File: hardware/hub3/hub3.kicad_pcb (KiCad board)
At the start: 2 copper layers, 42 x 42 mm, 11 parts, among them J1 LCD0, J2 LCD1, J3 LCD2, U1 74HC138, U2 XIAO ESP32S3

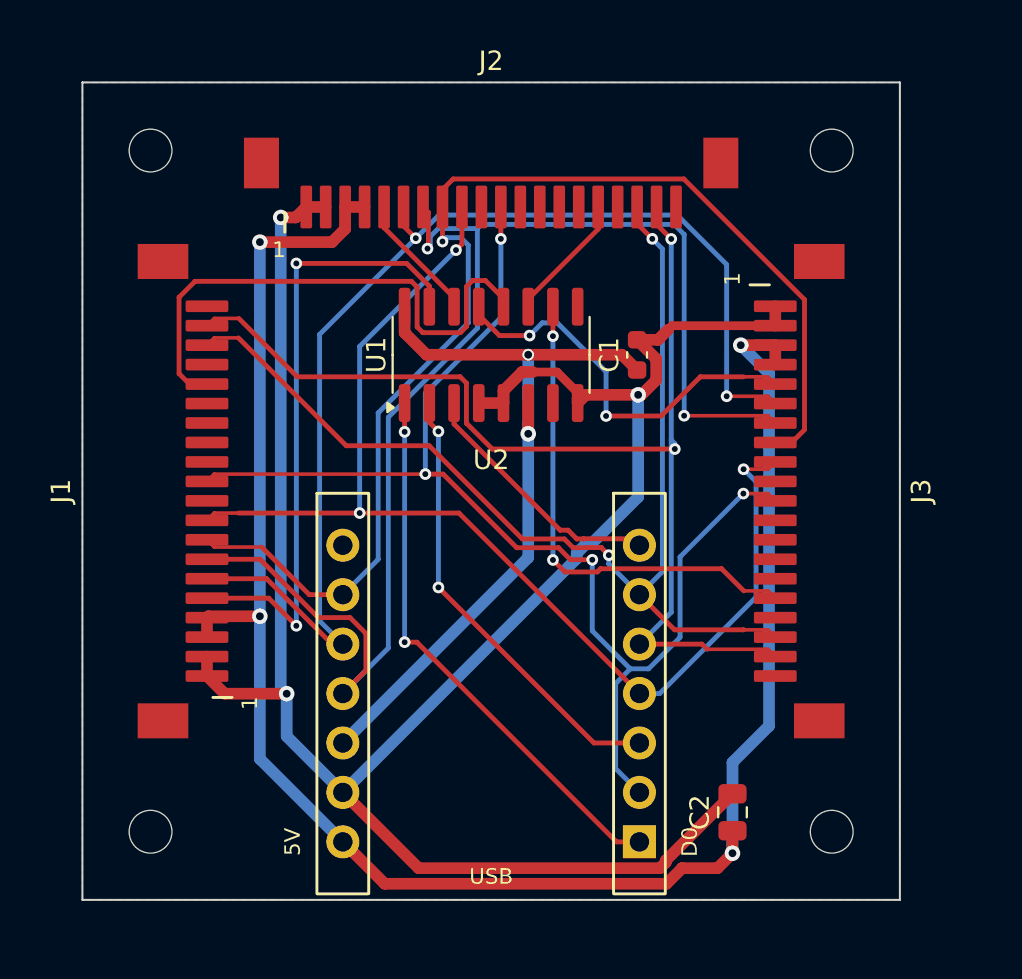
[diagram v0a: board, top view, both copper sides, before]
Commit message: hub3: route until clean, and write the JLCPCB files
Freerouting gives a different routing each run and now and then leaves
an island, a gap or a long neck on a power track, so route.py routes
again in a fresh process until KiCad's DRC is clean and the +5V and
+3V3 necks add up to 5 mm or less. GND pads join the pours directly.
fab.py writes the Gerbers, drill files, BOM and placement from the
board's lower left corner. Record why the FFC pin order is 1 to 1.

Claude-Session: https://claude.ai/code/session_01QQqL2MiTqB6ZDq8JiNUdWg
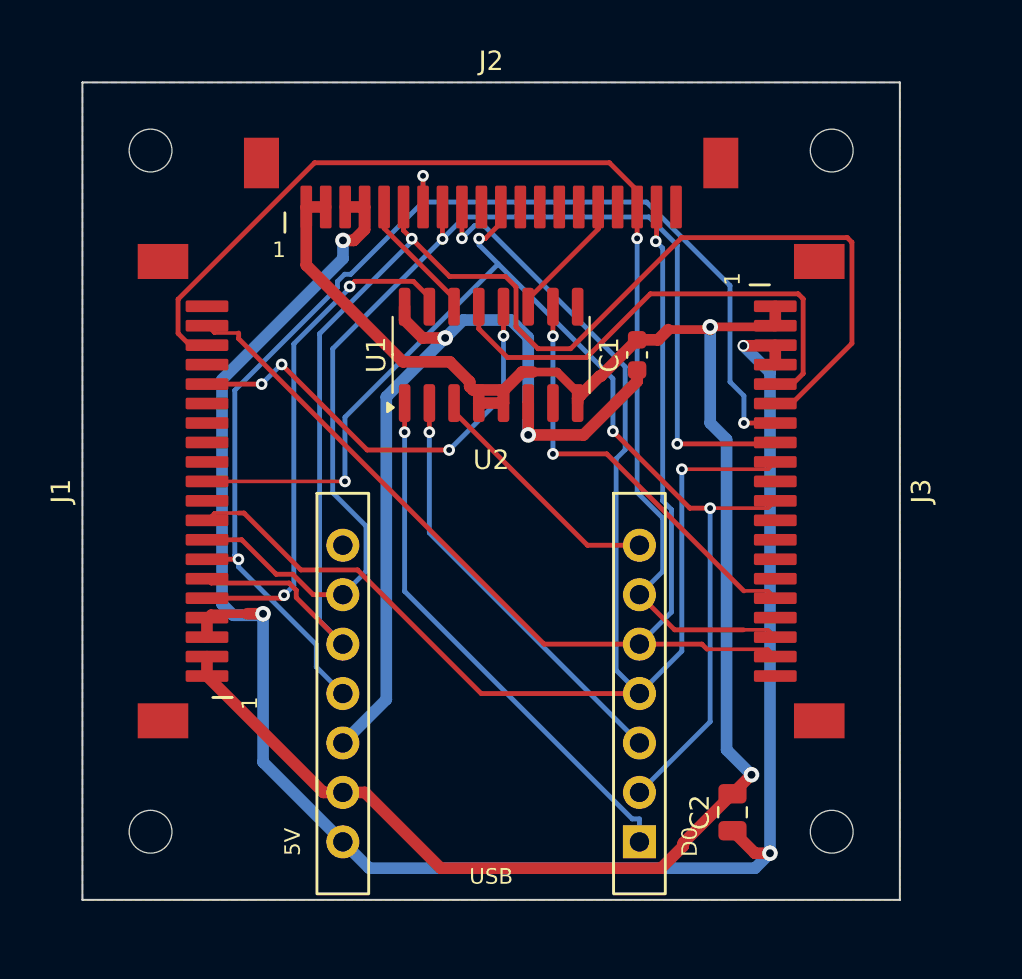
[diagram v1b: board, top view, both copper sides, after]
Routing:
- net GND: track 111.6 -> 95.8 mm, vias 3 -> 2
- net BL_CTRL: track 60.8 -> 74.3 mm, vias 3 -> 2
- net LCM_SDO: track 60.6 -> 72.7 mm, vias 2 -> 1
- net LCM_SDI: track 70.7 -> 62.8 mm, vias 2 -> 3
- net LCM_SCS0: track 32.2 -> 26.3 mm
- net +3V3: track 39.6 -> 45.1 mm
- net LCD_CS0: track 28.0 -> 23.2 mm, vias 0 -> 4
- net LCM_SCS2: track 20.7 -> 25.4 mm, vias 2 -> 0
- net LCD_CS2: track 25.4 -> 22.1 mm
- net LCD_DIN: track 56.9 -> 60.3 mm, vias 2 -> 1
- net +5V: track 96.1 -> 99.0 mm
- net LCM_SCLK: track 62.9 -> 60.0 mm, vias 1 -> 2
- net LCM_RESET: track 64.4 -> 62.8 mm
- net SEL_B: track 23.3 -> 21.9 mm, vias 2 -> 1
- net SEL_A: track 28.6 -> 27.8 mm, vias 2 -> 1
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
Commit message: hub3: use the Ckmtw C132515 FFC connector, 44 mm board
C132515 has JLCPCB's own EasyEDA footprint, so the pads come from it
rather than from pixels of a drawing. Its body is 2.5 mm longer, so the
board grows to 44 mm to keep the corners clear. Move the 10 uF next to
the XIAO 5V pin.

route.py now starts each attempt from an unrouted copy that make.py
leaves in build/ with the project beside it (without it pcbnew used the
default net classes and saved them over the project), and when an
attempt is not clean it makes the board again: Freerouting routes the
same DSN the same way whatever its options, but each make.py run gives
a different DSN. Allow 7.5 mm of necked power track, about 2.5 mm per
connector.

Claude-Session: https://claude.ai/code/session_01QQqL2MiTqB6ZDq8JiNUdWg
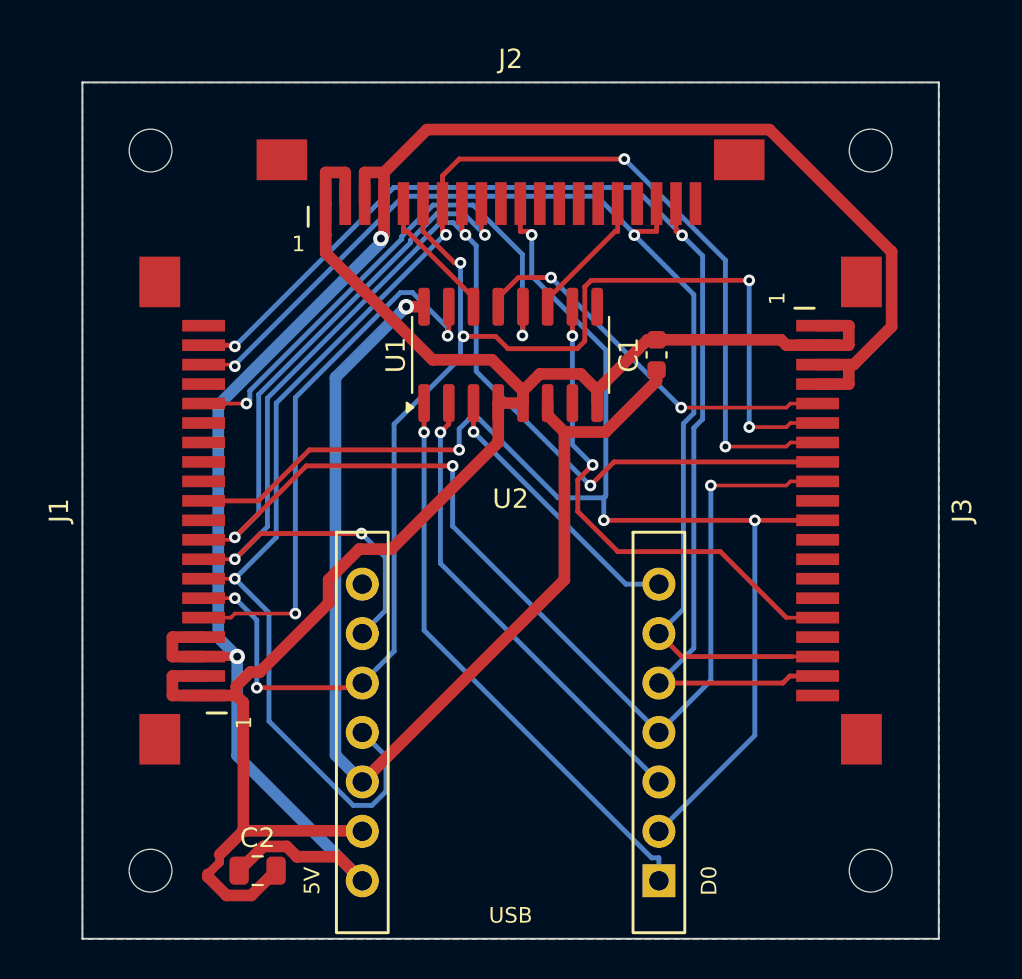
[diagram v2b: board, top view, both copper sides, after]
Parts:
- J1, J2, J3: footprint cubic-earth:FFC_1.0mm_20P_Bottom_C2998680 -> cubic-earth:FFC_1.0mm_20P_Bottom_C132515
- moved C2 24.6 mm to (109.0, 140.5), turned to 0 degrees
- moved H4 2.83 mm to (140.5, 140.5)
- moved J3 2.33 mm to (138.6, 122.0)
- moved U2 2.24 mm to (122.0, 133.4)
- moved H2 2.00 mm to (140.5, 103.5)
- moved H3 2.00 mm to (103.5, 140.5)
- moved J1 1.00 mm to (105.4, 122.0)
- moved J2 1.00 mm to (122.0, 105.4)
- moved C1 1.00 mm to (129.5, 114.0)
- moved U1 1.00 mm to (122.0, 114.0)
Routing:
- net LCM_SDI: track 62.8 -> 78.1 mm, vias 3 -> 4
- net +3V3: track 45.1 -> 57.9 mm, vias 2 -> 1
- net LCM_RESET: track 62.8 -> 72.0 mm
- net LCM_SCLK: track 60.0 -> 67.4 mm, vias 2 -> 4
- net LCM_SCS2: track 25.4 -> 20.2 mm, vias 0 -> 2
- net LCD_CS0: track 23.2 -> 27.7 mm, vias 4 -> 2
- net LCD_CS2: track 22.1 -> 25.9 mm
- net GND: track 95.8 -> 92.1 mm, vias 2 -> 0
- net LCD_SCLK: track 59.9 -> 63.5 mm, vias 1 -> 2
- net LCM_SDO: track 72.7 -> 69.2 mm, vias 1 -> 6
- net BL_CTRL: track 74.3 -> 77.4 mm, vias 2 -> 4
- net SEL_B: track 21.9 -> 24.3 mm
- net LCM_SCS0: track 26.3 -> 28.6 mm
- net SEL_A: track 27.8 -> 29.8 mm
- net SEL_C: track 12.8 -> 14.2 mm, vias 0 -> 1
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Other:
- board size 42 x 42 mm -> 44 x 44 mm

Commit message: hub3: assemble the XIAO's two pin sockets too
Replace the XIAO footprint with two 1x7 2.54 mm female sockets (J4, J5,
XFCN PM254V-11-07-H85, LCSC C2832270) for JLCPCB to fit. The XIAO
stays on the schematic but off the board; a board-only outline marks
where it sits and which row is D0 and which 5V. The placement file
gives the sockets' pad centre, since their origin is on pin 1. A test
checks the rows are 15.24 mm apart with D0 and 5V at the USB end.

Claude-Session: https://claude.ai/code/session_01QQqL2MiTqB6ZDq8JiNUdWg
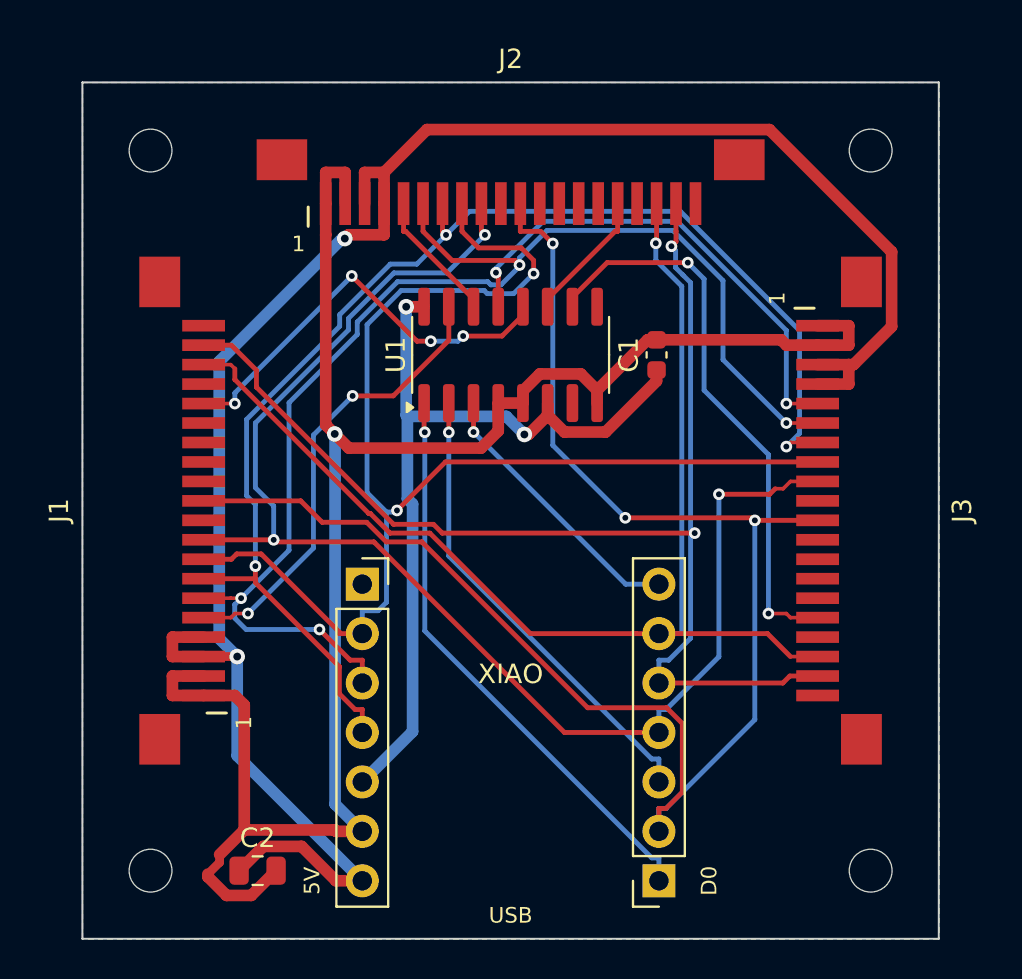
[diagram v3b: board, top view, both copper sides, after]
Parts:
- removed U2: XIAO ESP32S3, cubic-earth:XIAO_Socket_2x7_P2.54mm
- added J4: XIAO D0-D6, Connector_PinSocket_2.54mm:PinSocket_1x07_P2.54mm_Vertical, F.Cu at (129.6, 141.0)
- added J5: XIAO D7-5V, Connector_PinSocket_2.54mm:PinSocket_1x07_P2.54mm_Vertical, F.Cu at (114.4, 125.8)
- added X1: XIAO, cubic-earth:XIAO_ESP32S3_Outline, F.Cu at (122.0, 133.4)
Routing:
- net +3V3: track 57.9 -> 42.8 mm, vias 1 -> 2
- net LCM_SDI: track 78.1 -> 66.8 mm, vias 4 -> 3
- net LCM_RESET: track 72.0 -> 82.8 mm, vias 4 -> 3
- net BL_CTRL: track 77.4 -> 70.8 mm, vias 4 -> 3
- net GND: track 92.1 -> 98.2 mm, vias 0 -> 1
- net LCD_CS0: track 27.7 -> 21.8 mm, vias 2 -> 4
- net LCM_SCS2: track 20.2 -> 25.6 mm
- net LCM_SCS0: track 28.6 -> 23.6 mm
- net LCD_CS2: track 25.9 -> 29.5 mm
- net LCD_DIN: track 60.5 -> 61.9 mm, vias 2 -> 1
- net LCM_SDO: track 69.2 -> 67.9 mm, vias 6 -> 4
- net +5V: track 99.8 -> 100.9 mm
- net LCD_SCLK: track 63.5 -> 64.4 mm
- net LCM_SCLK: track 67.4 -> 66.7 mm, vias 4 -> 2
